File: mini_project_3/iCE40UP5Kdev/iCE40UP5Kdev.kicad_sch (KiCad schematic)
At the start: 51 parts, among them J1 USB4105-GF-A, J2 Left, J3 Right, U1 W25Q32JV, U2 MIC5365-1-2YD5, U3 MIC5318-3-3YD5, U4 ICE40UP5K-SG48ITR, X1 IQXO-791

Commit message: Set footprints for mini project 3
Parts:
- C1, C10, C11, C12, C13, C14, C15, C2, C3, C4, C5, C6, C7, C8, C9: footprint (none) -> Capacitor_SMD:C_0603_1608Metric
- D1, D2, D3, D5: footprint (none) -> LED_SMD:LED_0805_2012Metric
- D4: footprint (none) -> Diode_SMD:D_0603_1608Metric
- J1: footprint (none) -> Connector_USB:USB_C_Receptacle_GCT_USB4105-xx-A_16P_TopMnt_Horizontal
- J2, J3: footprint (none) -> Connector_PinHeader_2.54mm:PinHeader_1x20_P2.54mm_Vertical
- R1, R10, R11, R12, R13, R14, R15, R16, R17, R18, R19, R2, R20, R3, R4, R5, R6, R7, R8, R9: footprint (none) -> Resistor_SMD:R_0603_1608Metric
- S1, S2, S3: footprint (none) -> Button_Switch_SMD:SW_SPST_B3U-1000P
- U1: footprint (none) -> Package_SON:WSON-8-1EP_6x5mm_P1.27mm_EP3.4x4.3mm
- U2, U3: footprint (none) -> Package_TO_SOT_SMD:TSOT-23-5
- U4: footprint (none) -> Package_DFN_QFN:QFN-48-1EP_7x7mm_P0.5mm_EP5.6x5.6mm
- X1: footprint (none) -> Eclectronics:IQXO-791
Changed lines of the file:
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@@
 			)
 		)
-		(property "Footprint" ""
+		(property "Footprint" "Resistor_SMD:R_0603_1608Metric"
 			(at 194.31 184.912 90)
 			(effects
@@
 			)
 		)
-		(property "Footprint" ""
+		(property "Footprint" "Package_SON:WSON-8-1EP_6x5mm_P1.27mm_EP3.4x4.3mm"
 			(at 46.99 110.49 0)
 			(effects
@@
 			)
 		)
-		(property "Footprint" ""
+		(property "Footprint" "Resistor_SMD:R_0603_1608Metric"
 			(at 201.93 173.228 90)
 			(effects
@@
 			)
 		)
-		(property "Footprint" ""
+		(property "Footprint" "Diode_SMD:D_0603_1608Metric"
 			(at 123.19 130.81 0)
 			(effects
@@
 			)
 		)
-		(property "Footprint" ""
+		(property "Footprint" "Capacitor_SMD:C_0603_1608Metric"
 			(at 284.1752 33.02 0)
 			(effects
@@
 			)
 		)
-		(property "Footprint" ""
+		(property "Footprint" "Resistor_SMD:R_0603_1608Metric"
 			(at 194.31 179.832 90)
 			(effects
@@
 			)
 		)
-		(property "Footprint" ""
+		(property "Footprint" "Capacitor_SMD:C_0603_1608Metric"
 			(at 82.8548 59.69 0)
 			(effects
@@
 			)
 		)
-		(property "Footprint" ""
+		(property "Footprint" "LED_SMD:LED_0805_2012Metric"
 			(at 300.99 59.055 0)
 			(effects
@@
 			)
 		)
-		(property "Footprint" ""
+		(property "Footprint" "Capacitor_SMD:C_0603_1608Metric"
 			(at 121.92 165.4048 0)
 			(effects
@@
 			)
 		)
-		(property "Footprint" ""
+		(property "Footprint" "Resistor_SMD:R_0603_1608Metric"
 			(at 64.77 128.778 90)
 			(effects
@@
 			)
 		)
-		(property "Footprint" ""
+		(property "Footprint" "Resistor_SMD:R_0603_1608Metric"
 			(at 118.11 66.548 90)
 			(effects
@@
 			)
 		)
-		(property "Footprint" ""
+		(property "Footprint" "Capacitor_SMD:C_0603_1608Metric"
 			(at 121.92 124.7648 0)
 			(effects
@@
 			)
 		)
-		(property "Footprint" ""
+		(property "Footprint" "Resistor_SMD:R_0603_1608Metric"
 			(at 214.63 163.068 90)
 			(effects
@@
 			)
 		)
-		(property "Footprint" ""
+		(property "Footprint" "Capacitor_SMD:C_0603_1608Metric"
 			(at 121.92 175.5648 0)
 			(effects
@@
 			)
 		)
-		(property "Footprint" ""
+		(property "Footprint" "Resistor_SMD:R_0603_1608Metric"
 			(at 118.745 41.148 90)
 			(effects
@@
 			)
 		)
-		(property "Footprint" ""
+		(property "Footprint" "Resistor_SMD:R_0603_1608Metric"
 			(at 248.412 57.785 90)
 			(effects
@@
 			)
 		)
-		(property "Footprint" ""
+		(property "Footprint" "Connector_PinHeader_2.54mm:PinHeader_1x20_P2.54mm_Vertical"
 			(at 248.92 127 0)
 			(effects
@@
 			)
 		)
-		(property "Footprint" ""
+		(property "Footprint" "Resistor_SMD:R_0603_1608Metric"
 			(at 68.072 101.6 90)
 			(effects
@@
 			)
 		)
-		(property "Footprint" ""
+		(property "Footprint" "LED_SMD:LED_0805_2012Metric"
 			(at 201.93 186.69 0)
 			(effects
@@
 			)
 		)
-		(property "Footprint" ""
+		(property "Footprint" "Capacitor_SMD:C_0603_1608Metric"
 			(at 121.92 114.6048 0)
 			(effects
@@
 			)
 		)
-		(property "Footprint" ""
+		(property "Footprint" "Connector_PinHeader_2.54mm:PinHeader_1x20_P2.54mm_Vertical"
 			(at 297.18 127 0)
 			(effects
@@
 			)
 		)
-		(property "Footprint" ""
+		(property "Footprint" "Connector_USB:USB_C_Receptacle_GCT_USB4105-xx-A_16P_TopMnt_Horizontal"
 			(at 34.29 34.29 0)
 			(effects
@@
 			)
 		)
-		(property "Footprint" ""
+		(property "Footprint" "Capacitor_SMD:C_0603_1608Metric"
 			(at 121.92 134.9248 0)
 			(effects
@@
 			)
 		)
-		(property "Footprint" ""
+		(property "Footprint" "Capacitor_SMD:C_0603_1608Metric"
 			(at 248.6152 33.02 0)
 			(effects
@@
 			)
 		)
-		(property "Footprint" ""
+		(property "Footprint" "Package_TO_SOT_SMD:TSOT-23-5"
 			(at 267.97 28.575 0)
 			(effects
@@
 			)
 		)
-		(property "Footprint" ""
+		(property "Footprint" "Resistor_SMD:R_0603_1608Metric"
 			(at 194.31 174.752 90)
 			(effects
@@
 			)
 		)
-		(property "Footprint" ""
+		(property "Footprint" "LED_SMD:LED_0805_2012Metric"
 			(at 201.93 176.53 0)
 			(effects
@@
 			)
 		)
-		(property "Footprint" ""
+		(property "Footprint" "Resistor_SMD:R_0603_1608Metric"
 			(at 124.968 171.45 90)
 			(effects
@@
 			)
 		)
-		(property "Footprint" ""
+		(property "Footprint" "LED_SMD:LED_0805_2012Metric"
 			(at 118.11 69.85 0)
 			(effects
@@
 			)
 		)
-		(property "Footprint" ""
+		(property "Footprint" "Package_DFN_QFN:QFN-48-1EP_7x7mm_P0.5mm_EP5.6x5.6mm"
 			(at 153.67 113.03 0)
 			(effects
@@
 			)
 		)
-		(property "Footprint" ""
+		(property "Footprint" "Button_Switch_SMD:SW_SPST_B3U-1000P"
 			(at 201.93 160.02 90)
 			(effects
@@
 			)
 		)
-		(property "Footprint" ""
+		(property "Footprint" "Capacitor_SMD:C_0603_1608Metric"
 			(at 251.1552 70.485 0)
 			(effects
@@
 			)
 		)
-		(property "Footprint" ""
+		(property "Footprint" "Resistor_SMD:R_0603_1608Metric"
 			(at 57.912 46.99 90)
 			(effects
@@
 			)
 		)
-		(property "Footprint" ""
+		(property "Footprint" "Resistor_SMD:R_0603_1608Metric"
 			(at 118.745 46.228 90)
 			(effects
@@
 			)
 		)
-		(property "Footprint" ""
+		(property "Footprint" "Resistor_SMD:R_0603_1608Metric"
 			(at 64.77 86.868 90)
 			(effects
@@
 			)
 		)
-		(property "Footprint" ""
+		(property "Footprint" "Resistor_SMD:R_0603_1608Metric"
 			(at 59.182 101.6 90)
 			(effects
@@
 			)
 		)
-		(property "Footprint" ""
+		(property "Footprint" "Button_Switch_SMD:SW_SPST_B3U-1000P"
 			(at 52.07 83.82 90)
 			(effects
@@
 			)
 		)
-		(property "Footprint" ""
+		(property "Footprint" "Button_Switch_SMD:SW_SPST_B3U-1000P"
 			(at 52.07 68.58 90)
 			(effects
@@
 			)
 		)
-		(property "Footprint" ""
+		(property "Footprint" "LED_SMD:LED_0805_2012Metric"
 			(at 201.93 181.61 0)
 			(effects
@@
 			)
 		)
-		(property "Footprint" ""
+		(property "Footprint" "LED_SMD:LED_0805_2012Metric"
 			(at 194.31 171.45 0)
 			(effects
@@
 			)
 		)
-		(property "Footprint" ""
+		(property "Footprint" "Capacitor_SMD:C_0603_1608Metric"
 			(at 121.92 155.2448 0)
 			(effects
@@
 			)
 		)
-		(property "Footprint" ""
+		(property "Footprint" "Resistor_SMD:R_0603_1608Metric"
 			(at 118.745 51.308 90)
 			(effects
@@
 			)
 		)
-		(property "Footprint" ""
+		(property "Footprint" "Capacitor_SMD:C_0603_1608Metric"
 			(at 291.7952 62.865 0)
 			(effects
@@
 			)
 		)
-		(property "Footprint" ""
+		(property "Footprint" "Eclectronics:IQXO-791"
 			(at 93.98 55.88 0)
 			(effects
@@
 			)
 		)
-		(property "Footprint" ""
+		(property "Footprint" "Resistor_SMD:R_0603_1608Metric"
 			(at 66.802 46.99 90)
 			(effects
@@
 			)
 		)
-		(property "Footprint" ""
+		(property "Footprint" "Capacitor_SMD:C_0603_1608Metric"
 			(at 21.8948 115.57 0)
 			(effects
@@
 			)
 		)
-		(property "Footprint" ""
+		(property "Footprint" "Resistor_SMD:R_0603_1608Metric"
 			(at 64.77 133.858 90)
 			(effects
@@
 			)
 		)
-		(property "Footprint" ""
+		(property "Footprint" "Resistor_SMD:R_0603_1608Metric"
 			(at 64.77 71.628 90)
 			(effects
@@
 			)
 		)
-		(property "Footprint" ""
+		(property "Footprint" "Capacitor_SMD:C_0603_1608Metric"
 			(at 121.92 145.0848 0)
 			(effects
@@
 			)
 		)
-		(property "Footprint" ""
+		(property "Footprint" "Package_TO_SOT_SMD:TSOT-23-5"
 			(at 267.97 58.42 0)
 			(effects
@@
 			)
 		)
-		(property "Footprint" ""
+		(property "Footprint" "Capacitor_SMD:C_0603_1608Metric"
 			(at 280.3652 70.485 0)
 			(effects
@@
 			)
 		)
-		(property "Footprint" ""
+		(property "Footprint" "Resistor_SMD:R_0603_1608Metric"
 			(at 299.212 66.675 90)
 			(effects
@@
 			)
 		)
-		(property "Footprint" ""
+		(property "Footprint" "Capacitor_SMD:C_0603_1608Metric"
 			(at 240.9952 62.865 0)
 			(effects

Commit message: Add start to layout of mini project 3
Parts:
- J1: footprint Connector_USB:USB_C_Receptacle_GCT_USB4105-xx-A_16P_TopMnt_Horizontal -> Eclectronics:USB4105-GF-A
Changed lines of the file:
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@@
 			)
 		)
-		(property "Footprint" "Connector_USB:USB_C_Receptacle_GCT_USB4105-xx-A_16P_TopMnt_Horizontal"
+		(property "Footprint" "Eclectronics:USB4105-GF-A"
 			(at 34.29 34.29 0)
 			(effects

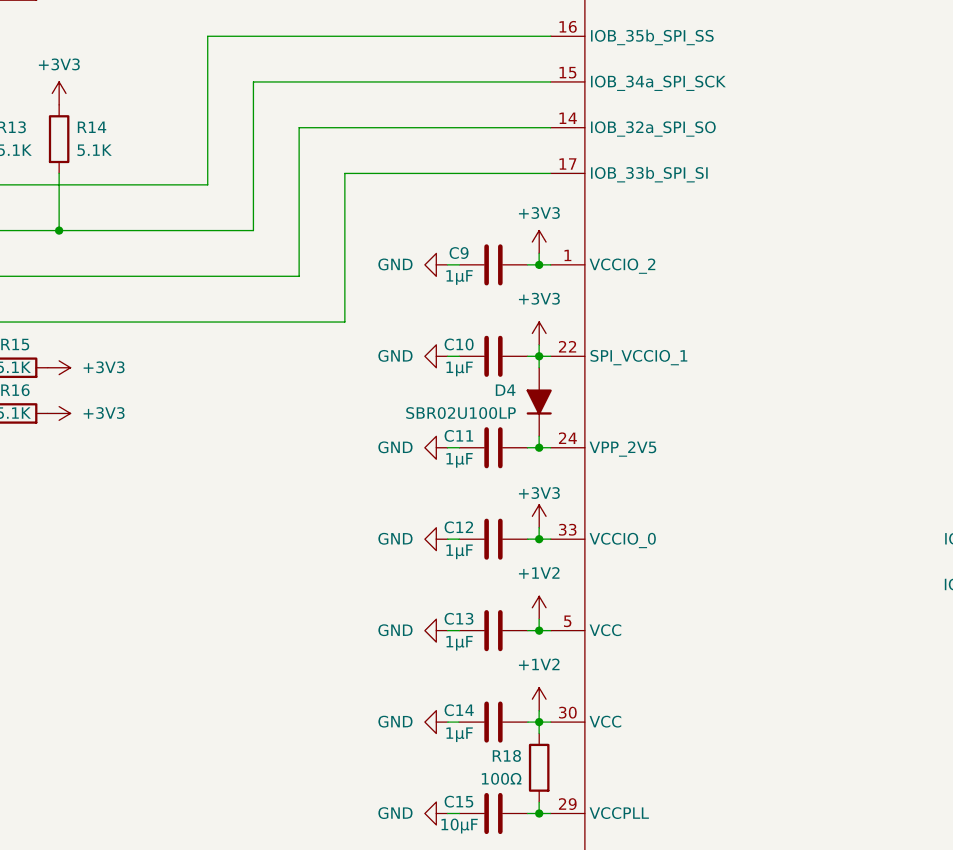
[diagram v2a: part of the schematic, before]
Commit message: Add more components to layout
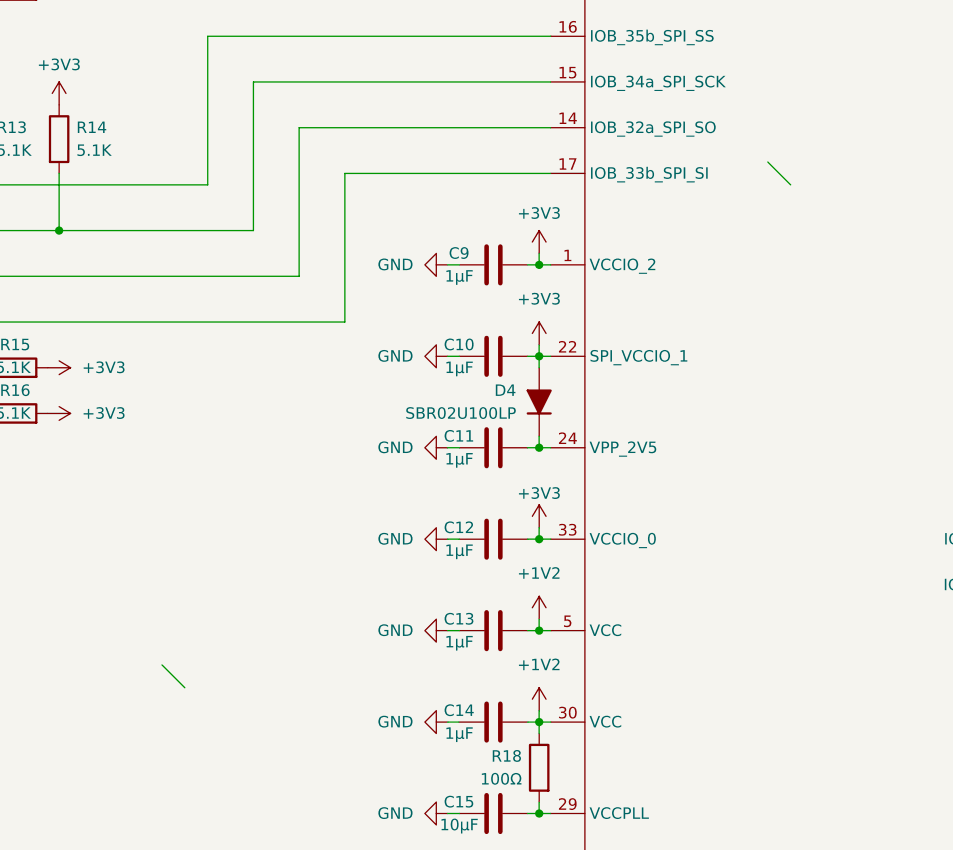
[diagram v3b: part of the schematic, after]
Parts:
- C10, C11, C12, C13, C14, C8, C9: footprint Capacitor_SMD:C_0603_1608Metric -> Capacitor_SMD:C_0402_1005Metric
- D4: footprint Diode_SMD:D_0603_1608Metric -> Diode_SMD:D_0402_1005Metric
- R10, R11, R12, R18: footprint Resistor_SMD:R_0603_1608Metric -> Resistor_SMD:R_0402_1005Metric
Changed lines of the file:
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@@
 		(at 102.87 52.07)
 	)
+	(bus_entry
+		(at 148.59 104.14)
+		(size 2.54 2.54)
+		(stroke
+			(width 0)
+			(type default)
+		)
+	)
+	(bus_entry
+		(at 81.28 160.02)
+		(size 2.54 2.54)
+		(stroke
+			(width 0)
+			(type default)
+		)
+	)
 	(wire
 		(pts
@@
 			)
 		)
-		(property "Footprint" "Diode_SMD:D_0603_1608Metric"
+		(property "Footprint" "Diode_SMD:D_0402_1005Metric"
 			(at 123.19 130.81 0)
 			(effects
@@
 			)
 		)
-		(property "Footprint" "Capacitor_SMD:C_0603_1608Metric"
+		(property "Footprint" "Capacitor_SMD:C_0402_1005Metric"
 			(at 82.8548 59.69 0)
 			(effects
@@
 			)
 		)
-		(property "Footprint" "Capacitor_SMD:C_0603_1608Metric"
+		(property "Footprint" "Capacitor_SMD:C_0402_1005Metric"
 			(at 121.92 165.4048 0)
 			(effects
@@
 			)
 		)
-		(property "Footprint" "Capacitor_SMD:C_0603_1608Metric"
+		(property "Footprint" "Capacitor_SMD:C_0402_1005Metric"
 			(at 121.92 124.7648 0)
 			(effects
@@
 			)
 		)
-		(property "Footprint" "Resistor_SMD:R_0603_1608Metric"
+		(property "Footprint" "Resistor_SMD:R_0402_1005Metric"
 			(at 118.745 41.148 90)
 			(effects
@@
 			)
 		)
-		(property "Footprint" "Capacitor_SMD:C_0603_1608Metric"
+		(property "Footprint" "Capacitor_SMD:C_0402_1005Metric"
 			(at 121.92 114.6048 0)
 			(effects
@@
 			)
 		)
-		(property "Footprint" "Capacitor_SMD:C_0603_1608Metric"
+		(property "Footprint" "Capacitor_SMD:C_0402_1005Metric"
 			(at 121.92 134.9248 0)
 			(effects
@@
 			)
 		)
-		(property "Footprint" "Resistor_SMD:R_0603_1608Metric"
+		(property "Footprint" "Resistor_SMD:R_0402_1005Metric"
 			(at 124.968 171.45 90)
 			(effects
@@
 			)
 		)
-		(property "Footprint" "Resistor_SMD:R_0603_1608Metric"
+		(property "Footprint" "Resistor_SMD:R_0402_1005Metric"
 			(at 118.745 46.228 90)
 			(effects
@@
 			)
 		)
-		(property "Footprint" "Capacitor_SMD:C_0603_1608Metric"
+		(property "Footprint" "Capacitor_SMD:C_0402_1005Metric"
 			(at 121.92 155.2448 0)
 			(effects
@@
 			)
 		)
-		(property "Footprint" "Resistor_SMD:R_0603_1608Metric"
+		(property "Footprint" "Resistor_SMD:R_0402_1005Metric"
 			(at 118.745 51.308 90)
 			(effects
@@
 			)
 		)
-		(property "Footprint" "Capacitor_SMD:C_0603_1608Metric"
+		(property "Footprint" "Capacitor_SMD:C_0402_1005Metric"
 			(at 121.92 145.0848 0)
 			(effects

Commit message: Add more layout progress
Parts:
- C7: footprint Capacitor_SMD:C_0603_1608Metric -> Capacitor_SMD:C_0402_1005Metric
- D1: footprint LED_SMD:LED_0805_2012Metric -> Eclectronics:IN-S85TATRGB
- R13, R14, R15, R16: footprint Resistor_SMD:R_0603_1608Metric -> Resistor_SMD:R_0402_1005Metric
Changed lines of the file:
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@@
 			)
 		)
-		(property "Footprint" "Resistor_SMD:R_0603_1608Metric"
+		(property "Footprint" "Resistor_SMD:R_0402_1005Metric"
 			(at 64.77 128.778 90)
 			(effects
@@
 			)
 		)
-		(property "Footprint" "Resistor_SMD:R_0603_1608Metric"
+		(property "Footprint" "Resistor_SMD:R_0402_1005Metric"
 			(at 68.072 101.6 90)
 			(effects
@@
 			)
 		)
-		(property "Footprint" "LED_SMD:LED_0805_2012Metric"
+		(property "Footprint" "Eclectronics:IN-S85TATRGB"
 			(at 201.93 186.69 0)
 			(effects
@@
 			)
 		)
-		(property "Footprint" "LED_SMD:LED_0805_2012Metric"
+		(property "Footprint" "Eclectronics:IN-S85TATRGB"
 			(at 201.93 176.53 0)
 			(effects
@@
 			)
 		)
-		(property "Footprint" "Resistor_SMD:R_0603_1608Metric"
+		(property "Footprint" "Resistor_SMD:R_0402_1005Metric"
 			(at 59.182 101.6 90)
 			(effects
@@
 			)
 		)
-		(property "Footprint" "LED_SMD:LED_0805_2012Metric"
+		(property "Footprint" "Eclectronics:IN-S85TATRGB"
 			(at 201.93 181.61 0)
 			(effects
@@
 			)
 		)
-		(property "Footprint" "Capacitor_SMD:C_0603_1608Metric"
+		(property "Footprint" "Capacitor_SMD:C_0402_1005Metric"
 			(at 21.8948 115.57 0)
 			(effects
@@
 			)
 		)
-		(property "Footprint" "Resistor_SMD:R_0603_1608Metric"
+		(property "Footprint" "Resistor_SMD:R_0402_1005Metric"
 			(at 64.77 133.858 90)
 			(effects

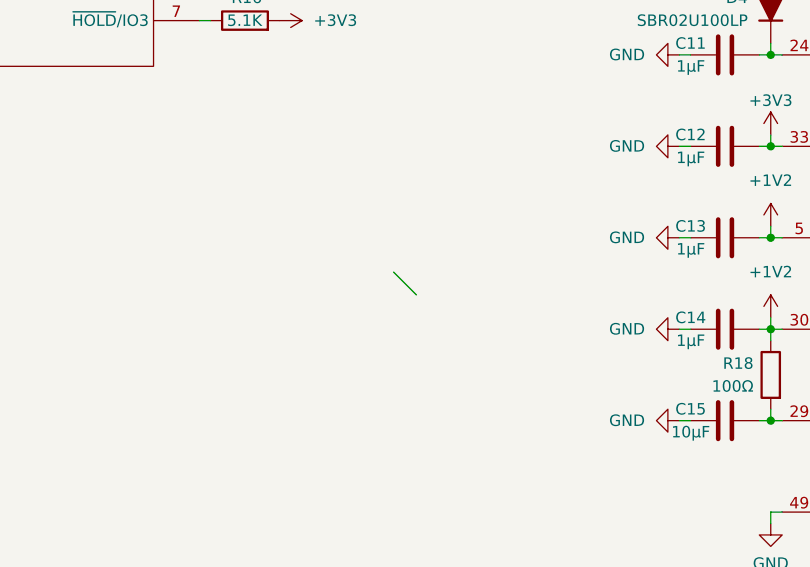
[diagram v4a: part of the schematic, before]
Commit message: Add layout with all components and most traces
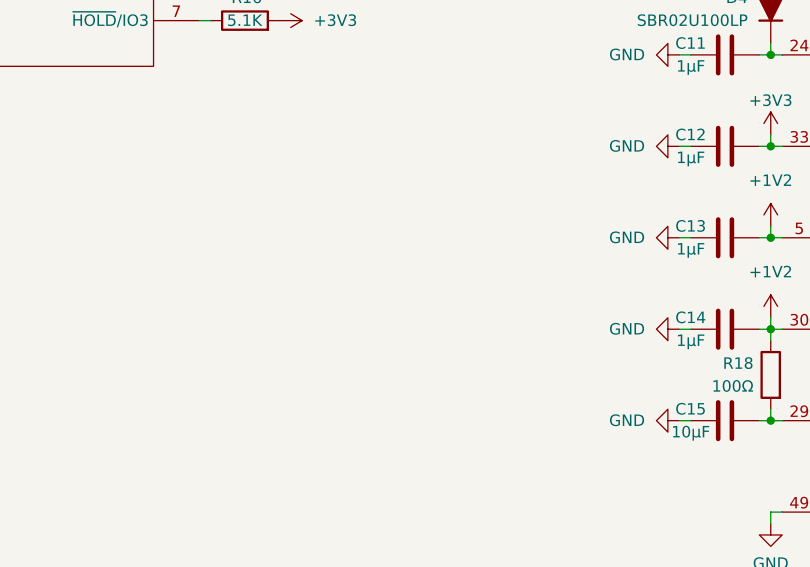
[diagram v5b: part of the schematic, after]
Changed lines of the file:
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@@
-		)
-	)
-	(bus_entry
-		(at 81.28 160.02)
-		(size 2.54 2.54)
-		(stroke
-			(width 0)
-			(type default)
 		)
 	)

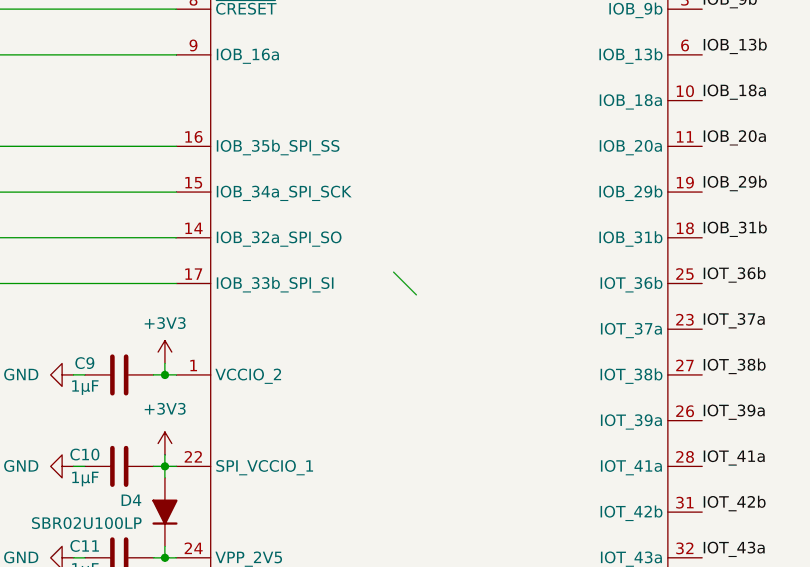
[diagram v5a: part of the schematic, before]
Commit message: Add silkscreen to mini project 3
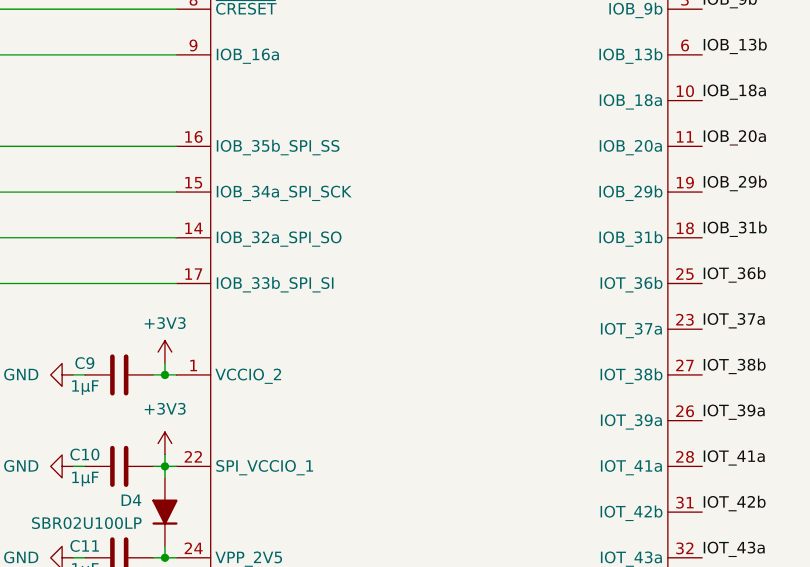
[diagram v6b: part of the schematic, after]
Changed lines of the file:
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@@
 		(at 102.87 52.07)
-	)
-	(bus_entry
-		(at 148.59 104.14)
-		(size 2.54 2.54)
-		(stroke
-			(width 0)
-			(type default)
-		)
 	)
 	(wire
